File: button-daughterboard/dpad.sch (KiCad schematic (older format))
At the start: 16 parts

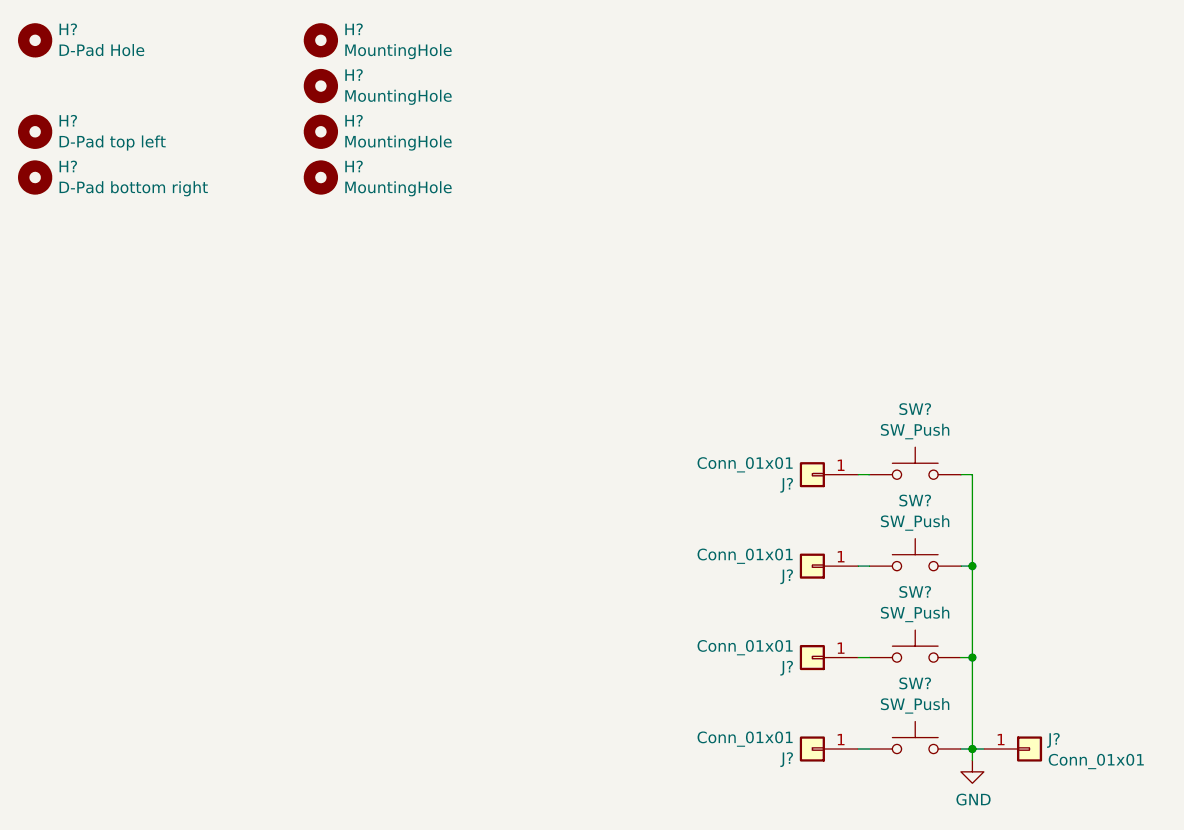
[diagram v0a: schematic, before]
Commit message: Add AB buttons
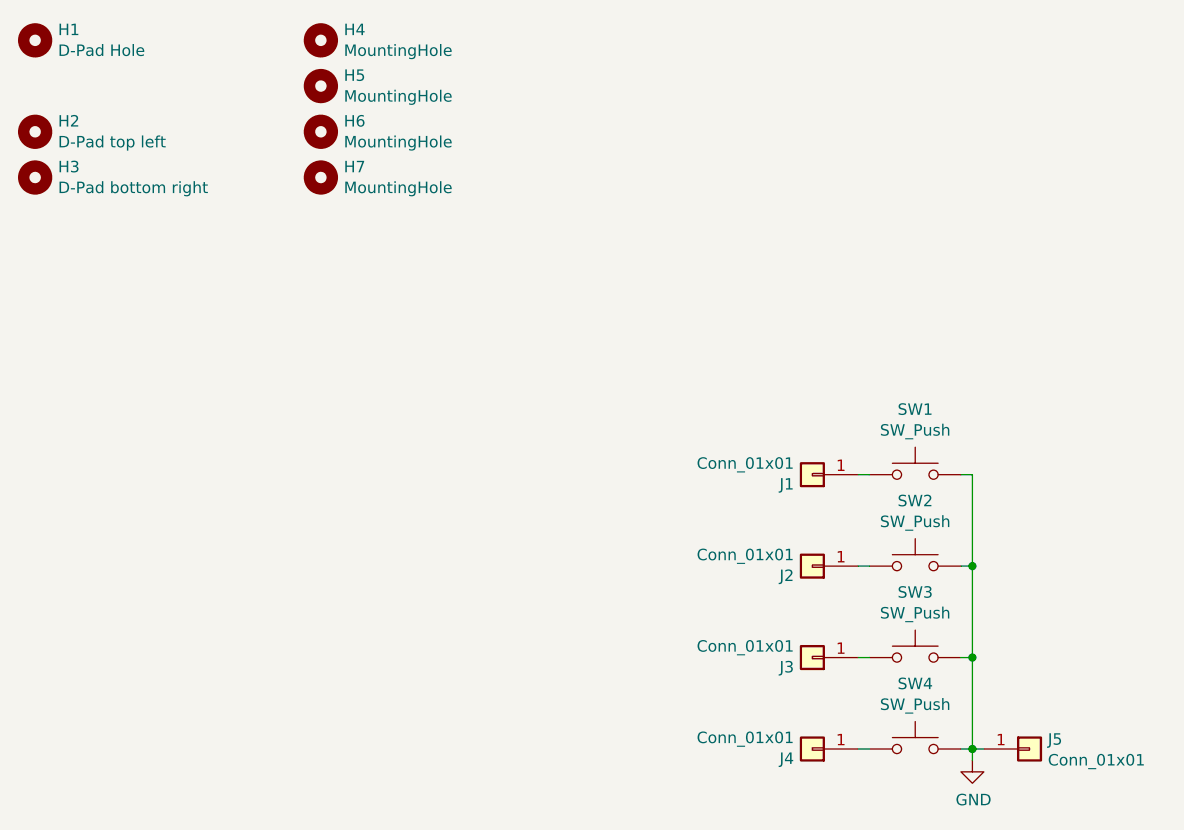
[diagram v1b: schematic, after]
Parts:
- H1: renamed from H?; footprint MountingHole:MountingHole_5mm -> MountingHole:MountingHole_5.5mm
- gave numbers to parts that had none: 15
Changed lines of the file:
@@
 $EndDescr
 $Comp
-L Switch:SW_Push SW?
+L Switch:SW_Push SW1
 U 1 1 60042157
 P 4650 2650
-F 0 "SW?" H 4650 2935 50  0000 C CNN
+F 0 "SW1" H 4650 2935 50  0000 C CNN
 F 1 "SW_Push" H 4650 2844 50  0000 C CNN
 F 2 "Button_Carbon:Button_Carbon_5mm" H 4650 2850 50  0001 C CNN
@@
 $EndComp
 $Comp
-L power:GND #PWR?
+L power:GND #PWR01
 U 1 1 60043235
 P 4900 3900
-F 0 "#PWR?" H 4900 3650 50  0001 C CNN
+F 0 "#PWR01" H 4900 3650 50  0001 C CNN
 F 1 "GND" H 4905 3727 50  0000 C CNN
 F 2 "" H 4900 3900 50  0001 C CNN
@@
 	4900 3850 4900 3450
 $Comp
-L Mechanical:MountingHole H?
+L Mechanical:MountingHole H1
 U 1 1 60043AA6
 P 800 750
-F 0 "H?" H 900 796 50  0000 L CNN
+F 0 "H1" H 900 796 50  0000 L CNN
 F 1 "D-Pad Hole" H 900 705 50  0000 L CNN
-F 2 "MountingHole:MountingHole_5mm" H 800 750 50  0001 C CNN
+F 2 "MountingHole:MountingHole_5.5mm" H 800 750 50  0001 C CNN
 F 3 "~" H 800 750 50  0001 C CNN
 	1    800  750
@@
 $EndComp
 $Comp
-L Mechanical:MountingHole H?
+L Mechanical:MountingHole H4
 U 1 1 60044384
 P 2050 750
-F 0 "H?" H 2150 796 50  0000 L CNN
+F 0 "H4" H 2150 796 50  0000 L CNN
 F 1 "MountingHole" H 2150 705 50  0000 L CNN
 F 2 "MountingHole:MountingHole_3.2mm_M3" H 2050 750 50  0001 C CNN
@@
 $EndComp
 $Comp
-L Mechanical:MountingHole H?
+L Mechanical:MountingHole H5
 U 1 1 6004493E
 P 2050 950
-F 0 "H?" H 2150 996 50  0000 L CNN
+F 0 "H5" H 2150 996 50  0000 L CNN
 F 1 "MountingHole" H 2150 905 50  0000 L CNN
 F 2 "MountingHole:MountingHole_3.2mm_M3" H 2050 950 50  0001 C CNN
@@
 $EndComp
 $Comp
-L Mechanical:MountingHole H?
+L Mechanical:MountingHole H6
 U 1 1 60044AA0
 P 2050 1150
-F 0 "H?" H 2150 1196 50  0000 L CNN
+F 0 "H6" H 2150 1196 50  0000 L CNN
 F 1 "MountingHole" H 2150 1105 50  0000 L CNN
 F 2 "MountingHole:MountingHole_3.2mm_M3" H 2050 1150 50  0001 C CNN
@@
 $EndComp
 $Comp
-L Mechanical:MountingHole H?
+L Mechanical:MountingHole H7
 U 1 1 60044BC5
 P 2050 1350
-F 0 "H?" H 2150 1396 50  0000 L CNN
+F 0 "H7" H 2150 1396 50  0000 L CNN
 F 1 "MountingHole" H 2150 1305 50  0000 L CNN
 F 2 "MountingHole:MountingHole_3.2mm_M3" H 2050 1350 50  0001 C CNN
@@
 $EndComp
 $Comp
-L Mechanical:MountingHole H?
+L Mechanical:MountingHole H2
 U 1 1 60045064
 P 800 1150
-F 0 "H?" H 900 1196 50  0000 L CNN
+F 0 "H2" H 900 1196 50  0000 L CNN
 F 1 "D-Pad top left" H 900 1105 50  0000 L CNN
 F 2 "MountingHole_GameBoy:MountingHole_GameBoy_DPAD" H 800 1150 50  0001 C CNN
@@
 $EndComp
 $Comp
-L Mechanical:MountingHole H?
+L Mechanical:MountingHole H3
 U 1 1 60045633
 P 800 1350
-F 0 "H?" H 900 1396 50  0000 L CNN
+F 0 "H3" H 900 1396 50  0000 L CNN
 F 1 "D-Pad bottom right" H 900 1305 50  0000 L CNN
 F 2 "MountingHole_GameBoy:MountingHole_GameBoy_DPAD" H 800 1350 50  0001 C CNN
@@
 $EndComp
 $Comp
-L Connector_Generic:Conn_01x01 J?
+L Connector_Generic:Conn_01x01 J5
 U 1 1 600460D9
 P 5150 3850
-F 0 "J?" H 5230 3892 50  0000 L CNN
+F 0 "J5" H 5230 3892 50  0000 L CNN
 F 1 "Conn_01x01" H 5230 3801 50  0000 L CNN
 F 2 "Connector_PinHeader_2.54mm:PinHeader_1x01_P2.54mm_Vertical" H 5150 3850 50  0001 C CNN
@@
 	4950 3850 4900 3850
 $Comp
-L Connector_Generic:Conn_01x01 J?
+L Connector_Generic:Conn_01x01 J4
 U 1 1 600468AB
 P 4200 3850
-F 0 "J?" H 4280 3892 50  0000 L CNN
+F 0 "J4" H 4280 3892 50  0000 L CNN
 F 1 "Conn_01x01" H 4280 3801 50  0000 L CNN
 F 2 "Connector_PinHeader_2.54mm:PinHeader_1x01_P2.54mm_Vertical" H 4200 3850 50  0001 C CNN
@@
 	4400 3850 4450 3850
 $Comp
-L Connector_Generic:Conn_01x01 J?
+L Connector_Generic:Conn_01x01 J3
 U 1 1 60046DFC
 P 4200 3450
-F 0 "J?" H 4280 3492 50  0000 L CNN
+F 0 "J3" H 4280 3492 50  0000 L CNN
 F 1 "Conn_01x01" H 4280 3401 50  0000 L CNN
 F 2 "Connector_PinHeader_2.54mm:PinHeader_1x01_P2.54mm_Vertical" H 4200 3450 50  0001 C CNN
@@
 	4400 3450 4450 3450
 $Comp
-L Connector_Generic:Conn_01x01 J?
+L Connector_Generic:Conn_01x01 J2
 U 1 1 60047092
 P 4200 3050
-F 0 "J?" H 4280 3092 50  0000 L CNN
+F 0 "J2" H 4280 3092 50  0000 L CNN
 F 1 "Conn_01x01" H 4280 3001 50  0000 L CNN
 F 2 "Connector_PinHeader_2.54mm:PinHeader_1x01_P2.54mm_Vertical" H 4200 3050 50  0001 C CNN
@@
 	4400 3050 4450 3050
 $Comp
-L Connector_Generic:Conn_01x01 J?
+L Connector_Generic:Conn_01x01 J1
 U 1 1 60047288
 P 4200 2650
-F 0 "J?" H 4280 2692 50  0000 L CNN
+F 0 "J1" H 4280 2692 50  0000 L CNN
 F 1 "Conn_01x01" H 4280 2601 50  0000 L CNN
 F 2 "Connector_PinHeader_2.54mm:PinHeader_1x01_P2.54mm_Vertical" H 4200 2650 50  0001 C CNN
@@
 	4400 2650 4450 2650
 $Comp
-L Switch:SW_Push SW?
+L Switch:SW_Push SW2
 U 1 1 600476D6
 P 4650 3050
-F 0 "SW?" H 4650 3335 50  0000 C CNN
+F 0 "SW2" H 4650 3335 50  0000 C CNN
 F 1 "SW_Push" H 4650 3244 50  0000 C CNN
 F 2 "Button_Carbon:Button_Carbon_5mm" H 4650 3250 50  0001 C CNN
@@
 $EndComp
 $Comp
-L Switch:SW_Push SW?
+L Switch:SW_Push SW3
 U 1 1 60047B41
 P 4650 3450
-F 0 "SW?" H 4650 3735 50  0000 C CNN
+F 0 "SW3" H 4650 3735 50  0000 C CNN
 F 1 "SW_Push" H 4650 3644 50  0000 C CNN
 F 2 "Button_Carbon:Button_Carbon_5mm" H 4650 3650 50  0001 C CNN
@@
 $EndComp
 $Comp
-L Switch:SW_Push SW?
+L Switch:SW_Push SW4
 U 1 1 60047FB1
 P 4650 3850
-F 0 "SW?" H 4650 4135 50  0000 C CNN
+F 0 "SW4" H 4650 4135 50  0000 C CNN
 F 1 "SW_Push" H 4650 4044 50  0000 C CNN
 F 2 "Button_Carbon:Button_Carbon_5mm" H 4650 4050 50  0001 C CNN
